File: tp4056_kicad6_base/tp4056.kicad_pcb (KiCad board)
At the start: 2 copper layers, 44 x 19 mm, 31 parts, among them J1 USB_B_Micro, J2 Conn_01x01_Female, J3 Conn_01x01_Female, J4 Conn_01x01_Female, J5 Conn_01x01_Female, J6 Conn_01x01_Female, J7 Conn_01x01_Female, J8 Conn_01x04_Male, Q1 FDN340P, Q2 FS8205A, U1 TP4056, U2 DW01, U3 LM1117-3.3, U4 LM809

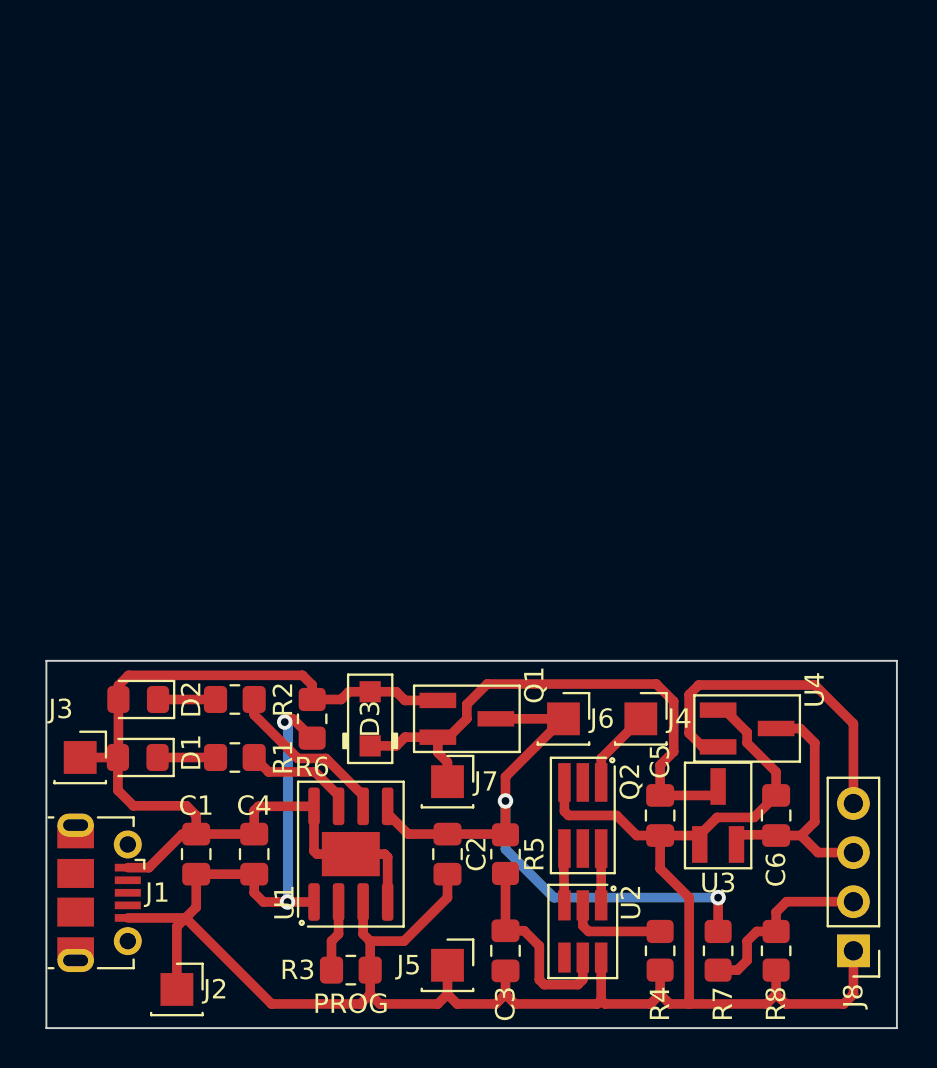
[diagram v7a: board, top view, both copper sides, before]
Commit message: pcb. new version 29x23. OJO Revisar disponibilidad de MOSFET!
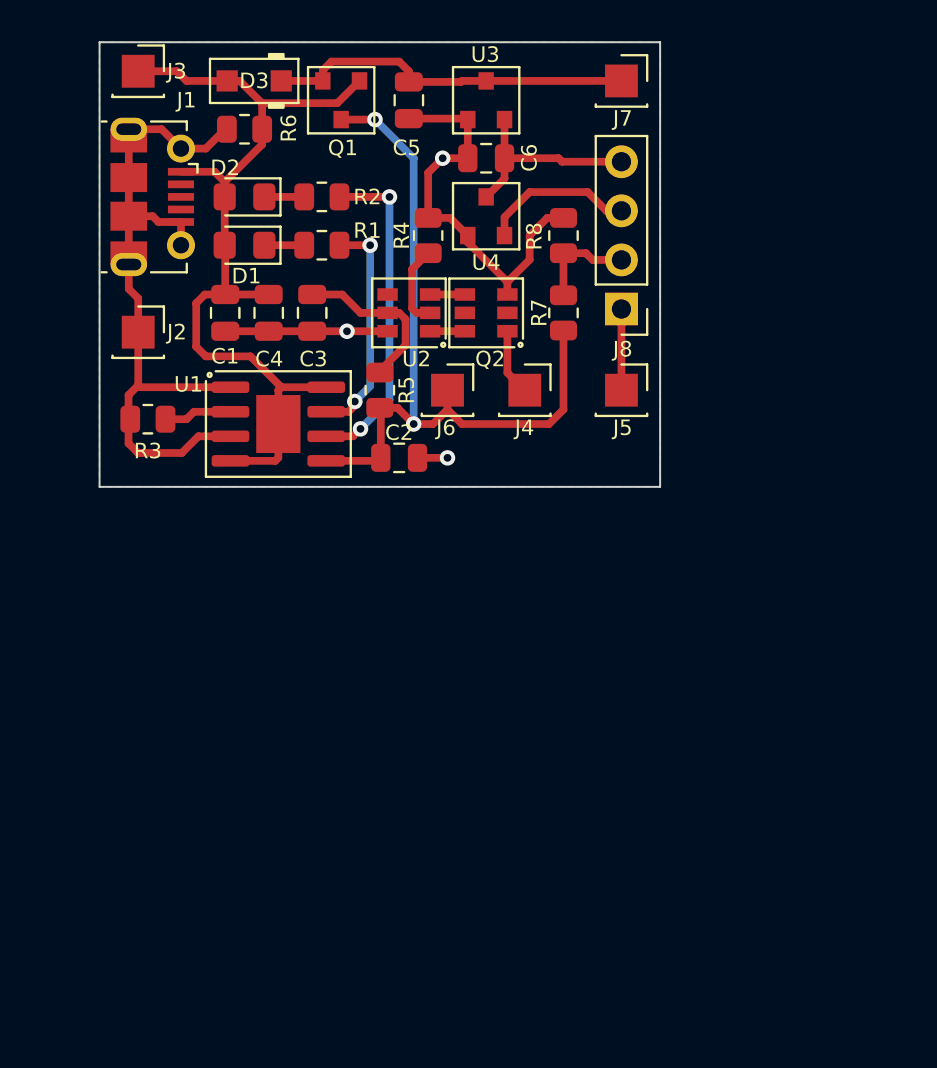
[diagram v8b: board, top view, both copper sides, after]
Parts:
- C1, C2, C3, C4, C5, C6: footprint Capacitor_SMD:C_0805_2012Metric_Pad1.18x1.45mm_HandSolder -> Capacitor_SMD:C_0805_2012Metric
- Q1, U3, U4: footprint Package_TO_SOT_SMD_AKL:SOT-23_Handsoldering -> Package_TO_SOT_SMD_AKL:SOT-23
- Q2: footprint Package_TO_SOT_SMD_AKL:TSOT-23-6_HandSoldering -> Package_TO_SOT_SMD_AKL:SOT-23-6
- R1, R2, R3, R4, R5, R6, R7, R8: footprint Resistor_SMD:R_0805_2012Metric_Pad1.20x1.40mm_HandSolder -> Resistor_SMD:R_0805_2012Metric
- U2: footprint Package_TO_SOT_SMD_AKL:SOT-23-6_Handsoldering -> Package_TO_SOT_SMD_AKL:SOT-23-6
- moved C5 39.2 mm to (136.0, 59.0)
- moved R4 38.9 mm to (137.0, 66.0), turned to -90 degrees
- moved U3 38.9 mm to (140.0, 59.0)
- moved R8 38.6 mm to (144.0, 66.0), turned to 90 degrees
- moved J7 37.4 mm to (147.0, 58.0)
- moved C6 37.2 mm to (140.0, 62.0), turned to 180 degrees
- moved J1 36.1 mm to (122.8, 64.0)
- moved J3 35.6 mm to (122.0, 57.5)
- moved J8 35.3 mm to (147.0, 69.8)
- moved C3 34.5 mm to (131.0, 70.0)
- moved J2 34.1 mm to (122.0, 71.0)
- moved R7 34.0 mm to (144.0, 70.0), turned to 90 degrees
- moved D3 33.5 mm to (128.0, 58.0), turned to 180 degrees
- moved U2 33.2 mm to (136.0, 70.0), turned to 180 degrees
- moved Q1 32.7 mm to (132.5, 59.0), turned to -90 degrees
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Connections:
- J1 pad 6: unconnected-(J1-Pad6) -> Earth
- J8 pad 3: +3.3V -> /RST
- J8 pad 4: /RST -> +3.3V
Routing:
- net Earth: track 116.5 -> 71.1 mm, vias 2 -> 3
- net /RST: track 17.5 -> 7.94 mm
- net /OUT+: track 28.5 -> 19.1 mm
- net Net-(R2-Pad2): track 8.71 -> 17.1 mm, vias 0 -> 2
- net Net-(R1-Pad2): track 5.74 -> 12.0 mm, vias 0 -> 2
- net /BAT+: track 34.0 -> 39.7 mm
- net VBUS: track 51.2 -> 45.8 mm
- net /measurment: track 9.64 -> 5.32 mm
- net +3.3V: track 13.8 -> 10.5 mm
- net Net-(C3-Pad1): track 10.4 -> 8.58 mm
- net Net-(Q2-Pad4): track 2.94 -> 1.80 mm
- net Net-(Q2-Pad6): track 2.94 -> 1.80 mm
- net Net-(D1-Pad1): track 3.00 -> 1.97 mm
- net Net-(D2-Pad1): track 2.97 -> 1.97 mm
- net Net-(R4-Pad2): track 5.18 -> 4.23 mm
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- added copper zone on B.Cu, net Earth
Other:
- board size 44 x 19 mm -> 29 x 23 mm
